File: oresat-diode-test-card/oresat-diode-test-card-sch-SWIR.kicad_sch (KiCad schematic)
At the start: 13 parts, among them Q3 NMOS, Q4 DMP3050LVT-7, U4 TLV6001DCK

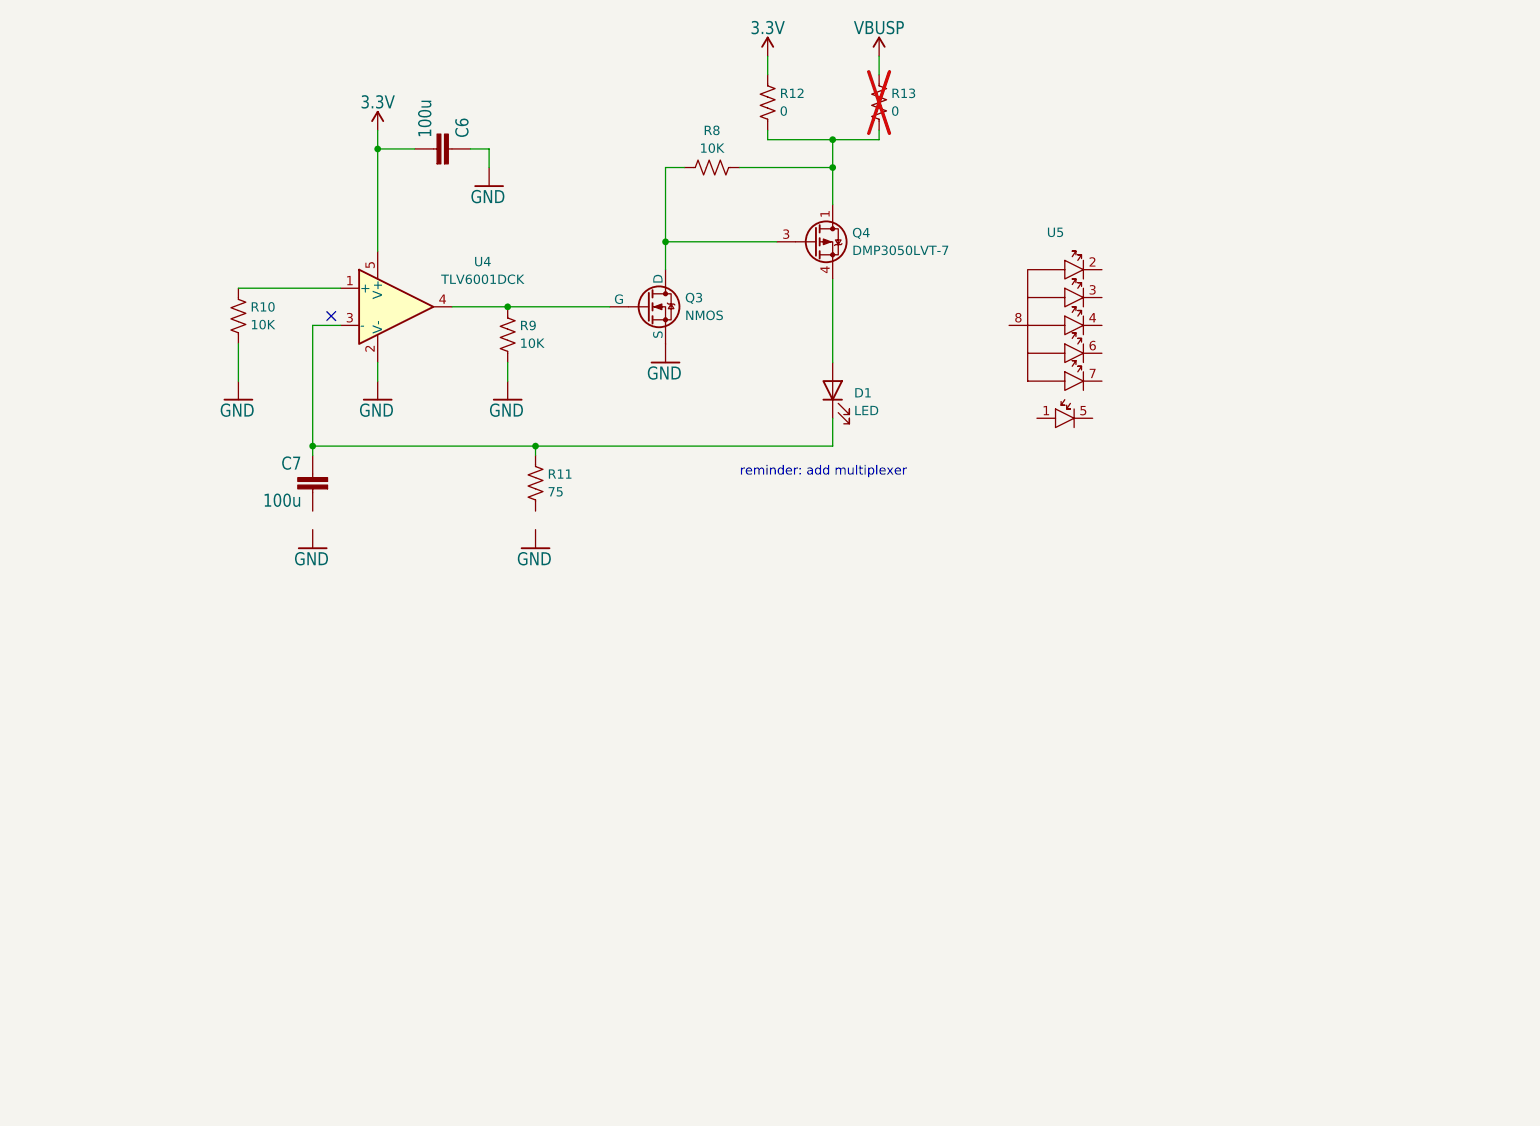
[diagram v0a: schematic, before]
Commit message: added photodiode and mux on schematic
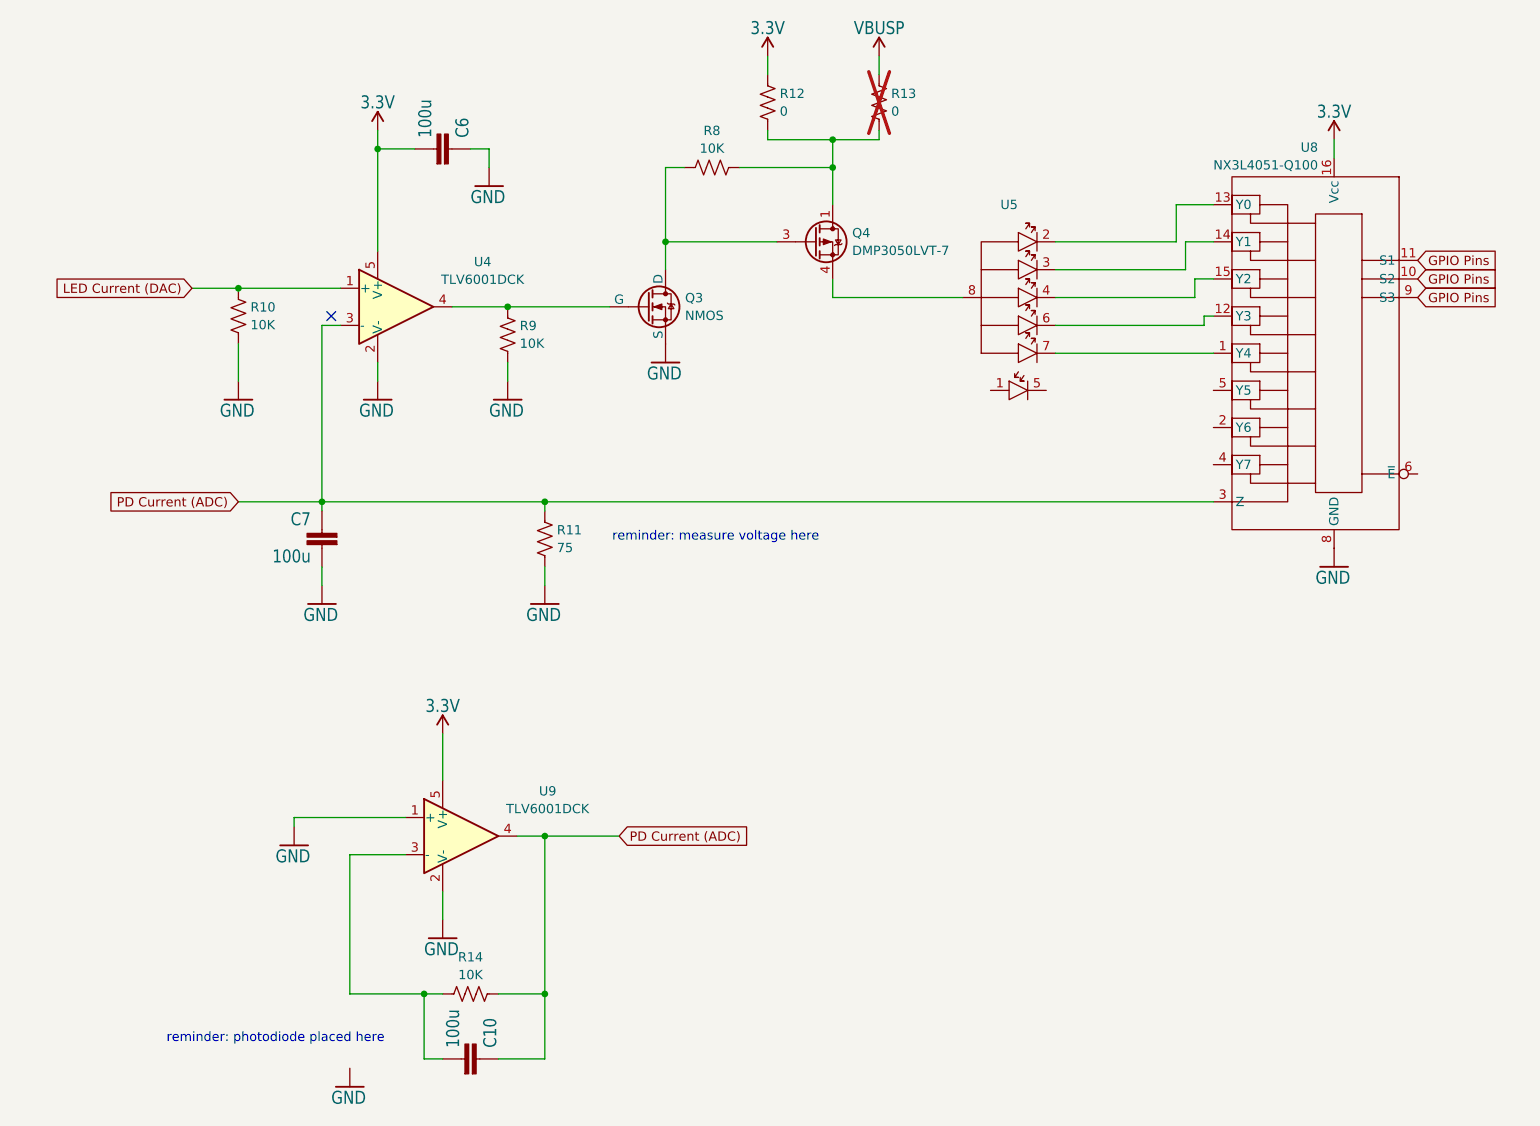
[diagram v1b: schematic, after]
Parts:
- removed D1: LED, symbol Device:LED
- added C10: 100u, oresat-passives:0603-C-NOSILK, symbol oresat-proto-card-eagle-import:C-EU0603-C-NOSILK
- added R14: 10K, symbol Device:R_US
- added U8: NX3L4051-Q100, Package_SO:TSSOP-16_4.4x5mm_P0.65mm, symbol oresat-ics:NX3L4051-Q100
- added U9: TLV6001DCK, Package_TO_SOT_SMD:SOT-353_SC-70-5, symbol Amplifier_Operational:TLV6001DCK
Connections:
- net 3.3V: now also U8.16 (Vcc), U9.5 (V+)
- net GND: now also C7.2, R11.1, U8.8 (GND), U9.1 (+), U9.2 (V-)
- net PD Current (ADC): now reaches C7.1, R11.2, U4.3 (-)
- net PD Current (ADC): now also C10.1, R14.2, U8.3 (Z), U9.4
- net at Q4.4 (S): now also U5.8 (LED_Anode_Com)
- net LED Current (DAC): now reaches R10.2, U4.1 (+)
- net at U5.2 (1040nm): now also U8.13 (Y0)
- net at U5.3 (1200nm): now also U8.14 (Y1)
- net at U5.4 (1300nm): now also U8.15 (Y2)
- net at U5.6 (1460nm): now also U8.12 (Y3)
- net at U5.7 (1550nm): now also U8.1 (Y4)
- new net: C10.2, R14.1, U9.3 (-)
- new net GPIO Pins: U8.10 (S2), U8.11 (S1), U8.9 (S3)
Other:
- note added: "reminder: measure voltage here"
- note added: "reminder: photodiode placed here"
- note removed: "reminder: add multiplexer"
- moved on the sheet: C7, R11, U5

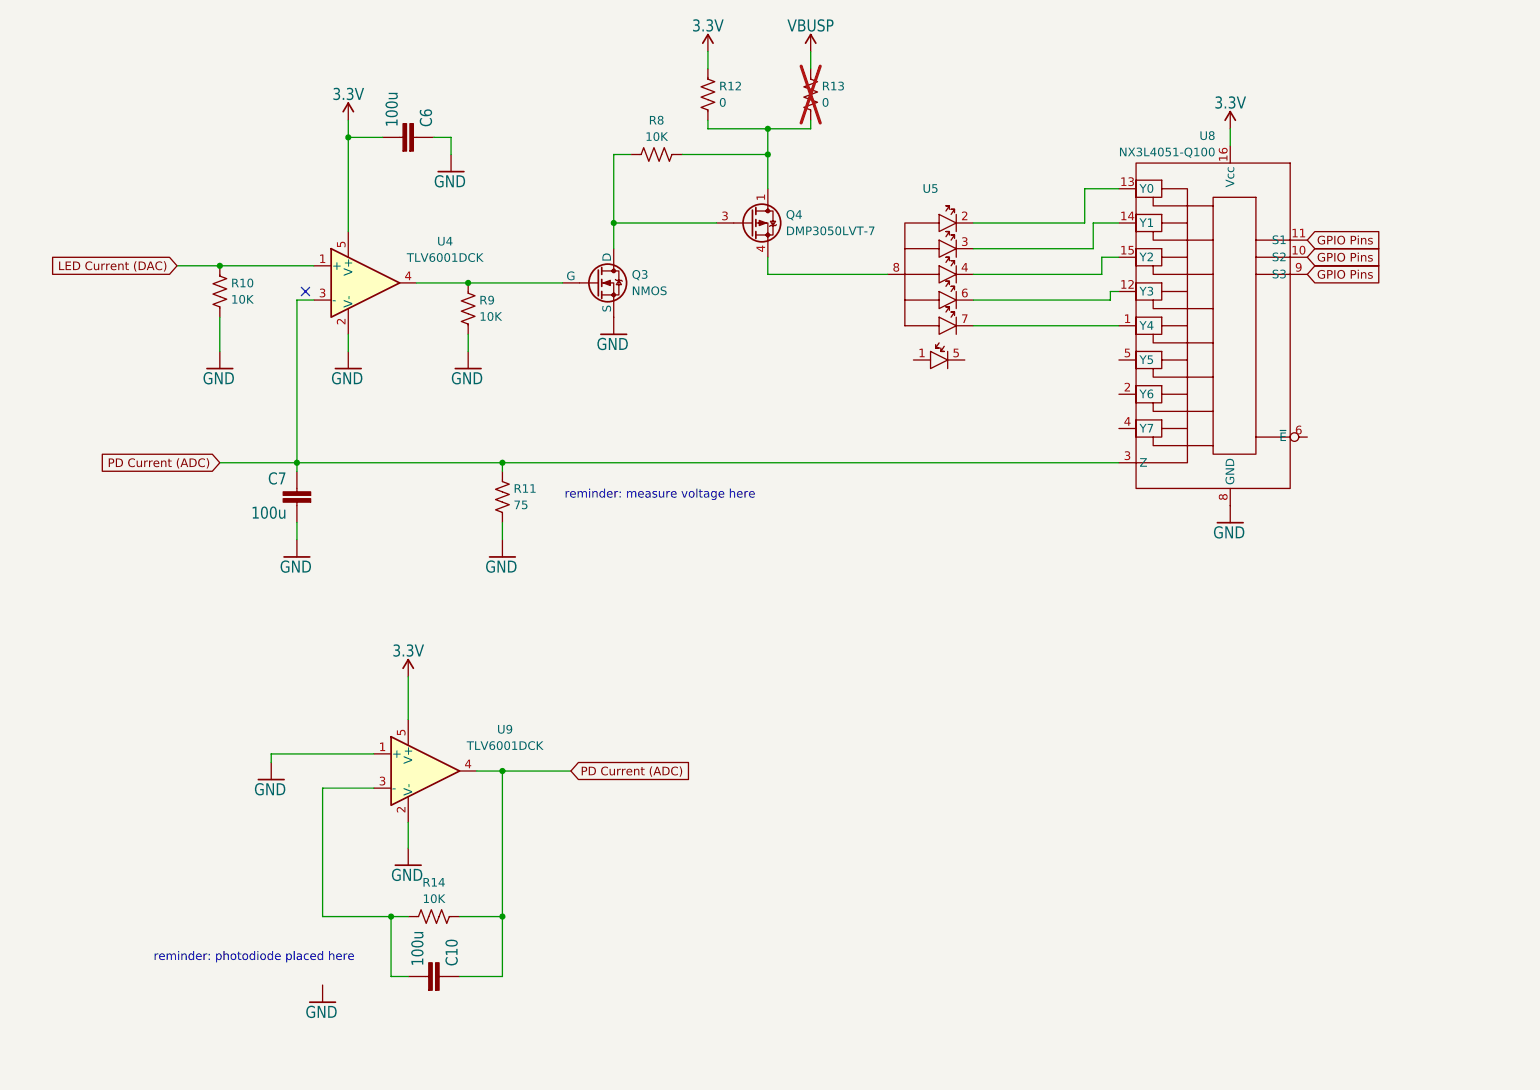
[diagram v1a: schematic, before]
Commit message: added additional LED and photodiode slots
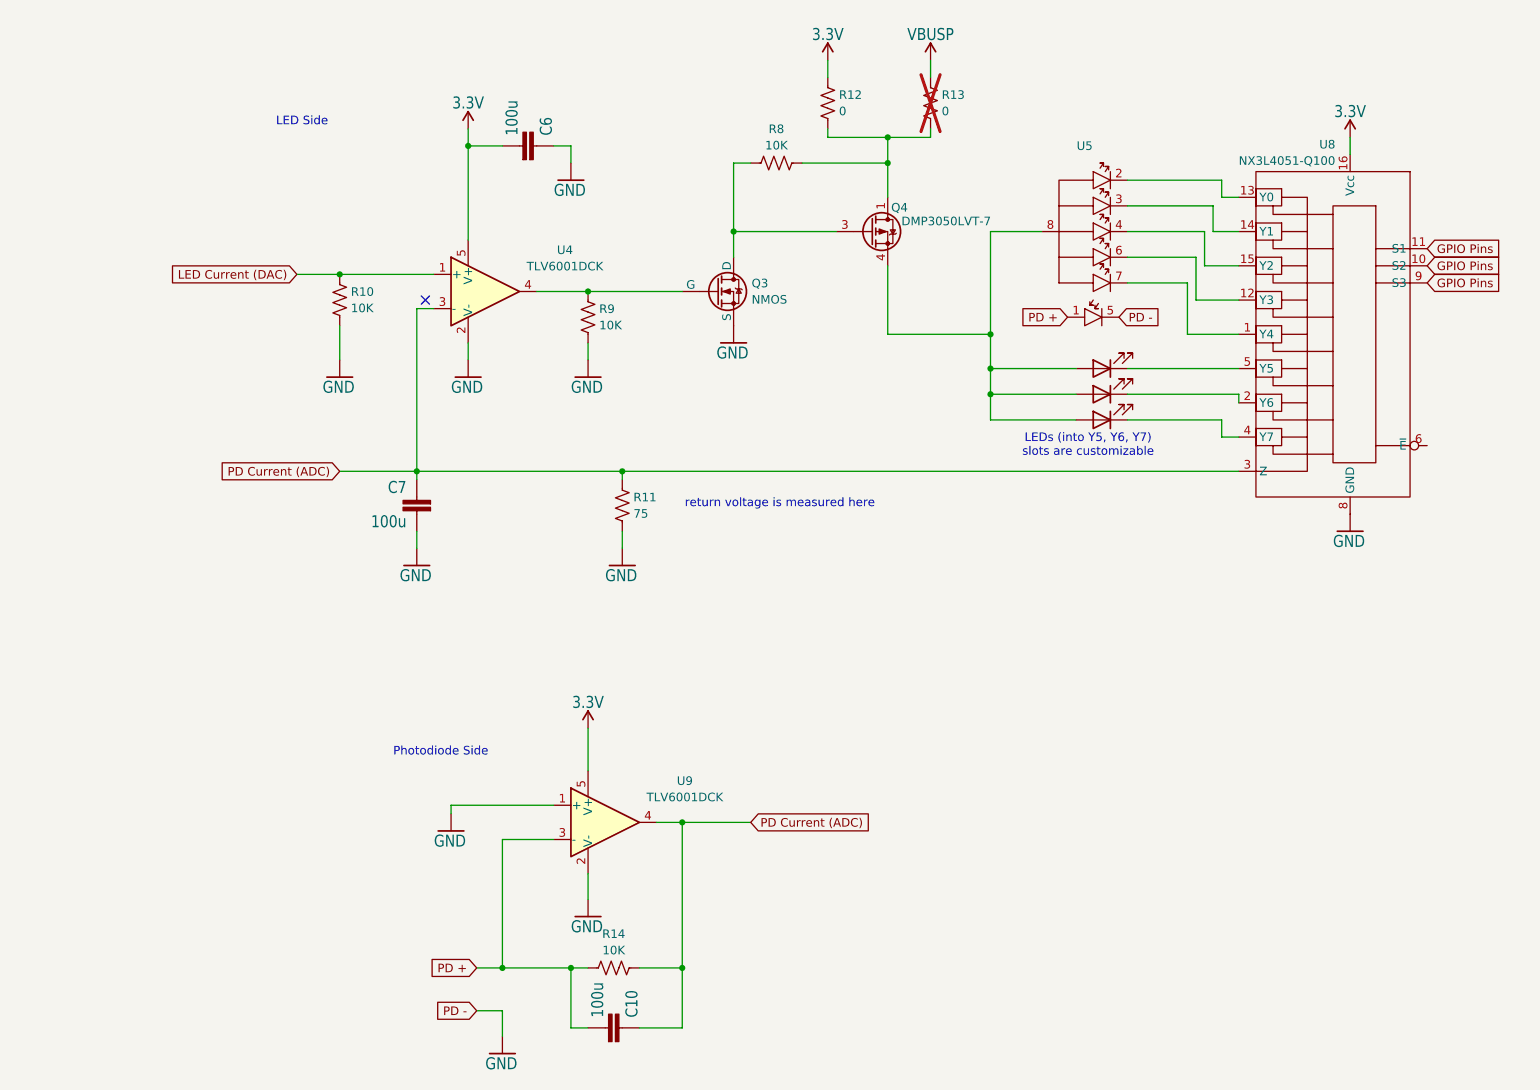
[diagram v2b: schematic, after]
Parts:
- added D1, D2, D4: LED, symbol Device:LED
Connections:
- net GND: now also U5.5 (PD_Cathode)
- net PD +: now reaches C10.2, R14.1, U9.3 (-)
- net PD +: now also U5.1 (PD_Anode)
- net at Q4.4 (S), U5.8 (LED_Anode_Com): now also D1.2 (A), D2.2 (A), D4.2 (A)
- net at U8.2 (Y6): now also D2.1 (K)
- net at U8.4 (Y7): now also D4.1 (K)
- net at U8.5 (Y5): now also D1.1 (K)
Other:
- note added: "LED Side"
- note added: "LEDs (into Y5, Y6, Y7) slots are customizable"
- note added: "Photodiode Side"
- note added: "return voltage is measured here"
- note removed: "reminder: measure voltage here"
- note removed: "reminder: photodiode placed here"
- moved on the sheet: C10, C6, C7, Q3, Q4, R10, R11, R12, R13, R14, R8, R9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
